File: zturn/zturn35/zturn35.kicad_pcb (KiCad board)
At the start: 4 copper layers, 189.9 x 54 mm, 50 parts, among them U1 74AXP4T245, U10 74AXP4T245, U11 74AXP4T245, U12 74AXP4T245, U2 74AXP4T245, U3 74AXP4T245, U4 74AXP4T245, U5 74AXP4T245, U6 74AXP4T245, U7 74AXP4T245, U8 74AXP4T245, U9 74AXP4T245

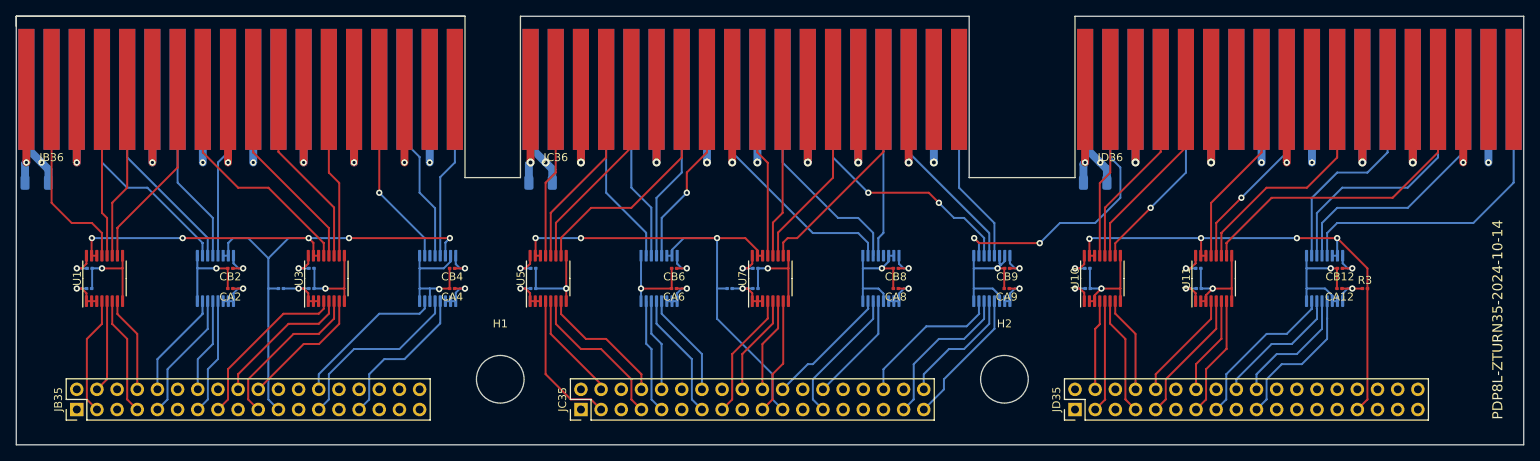
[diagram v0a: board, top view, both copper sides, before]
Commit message: update zturn34,35 pcbs - move 10uF caps, add fiducials
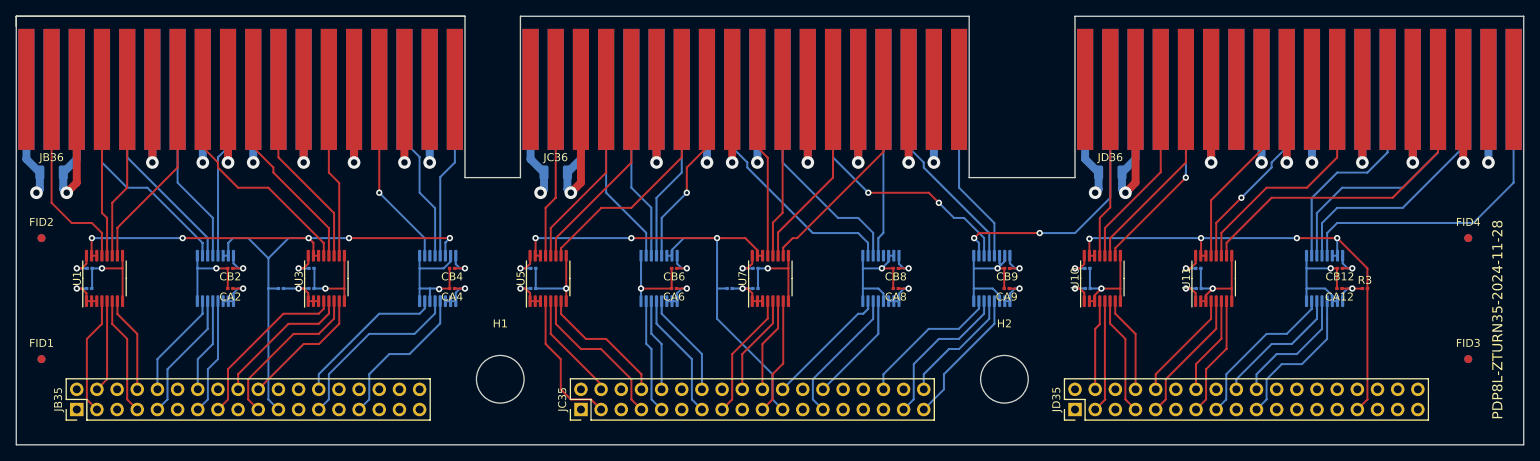
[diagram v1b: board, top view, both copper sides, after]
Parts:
- added FID1: Fiducial, Fiducial:Fiducial_1mm_Mask2mm, F.Cu at (3.17, 43.2)
- added FID2: Fiducial, Fiducial:Fiducial_1mm_Mask2mm, F.Cu at (3.17, 27.9)
- added FID3: Fiducial, Fiducial:Fiducial_1mm_Mask2mm, F.Cu at (182.9, 43.2)
- added FID4: Fiducial, Fiducial:Fiducial_1mm_Mask2mm, F.Cu at (182.9, 27.9)
- added FID5: Fiducial, Fiducial:Fiducial_1mm_Mask2mm, B.Cu at (3.17, 43.2)
- added FID6: Fiducial, Fiducial:Fiducial_1mm_Mask2mm, B.Cu at (3.17, 27.9)
- added FID7: Fiducial, Fiducial:Fiducial_1mm_Mask2mm, B.Cu at (182.9, 43.2)
- added FID8: Fiducial, Fiducial:Fiducial_1mm_Mask2mm, B.Cu at (182.9, 27.9)
- moved C3 2.29 mm to (137.8, 19.7), turned to 0 degrees
- moved C2 2.29 mm to (67.9, 19.7), turned to 0 degrees
- moved C1 2.26 mm to (4.45, 19.7), turned to 0 degrees
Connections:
- JB36 pad A1: GND -> unconnected-(JB36-PadA1)
- JC36 pad A1: GND -> unconnected-(JC36-PadA1)
- JD36 pad A1: GND -> unconnected-(JD36-PadA1)
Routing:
- net +5V: track 78.3 -> 103.3 mm
- net GND: track 433.9 -> 456.9 mm, vias 42 -> 39
- net /pBMB_10: track 33.5 -> 25.9 mm
- net /pBMB_02: track 17.6 -> 24.9 mm
- net /jTHREECYCLE: track 31.4 -> 24.1 mm
- net /jMEM03: track 29.5 -> 22.2 mm
- net /j_DMADATA_05: track 21.5 -> 14.2 mm
- net /j_EXTDMAADD_13: track 25.2 -> 17.9 mm
- net /j_DMADATA_04: track 23.3 -> 16.0 mm
- net /j_DMADATA_02: track 17.6 -> 24.9 mm
- net /jMEM04: track 24.9 -> 17.6 mm
- net /pBMB_07: track 24.6 -> 17.3 mm
- net /jMEM11: track 21.5 -> 14.2 mm
- net /pD35B2: track 37.7 -> 35.4 mm
- net /oD35B2: track 19.1 -> 18.3 mm
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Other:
- board text added: "PDP8L-ZTURN35-2024-11-28"
- board text removed: "PDP8L-ZTURN35-2024-10-14"

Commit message: use transistors for bus drivers instead of chips
to handle the 180 & 220-ohm pullups
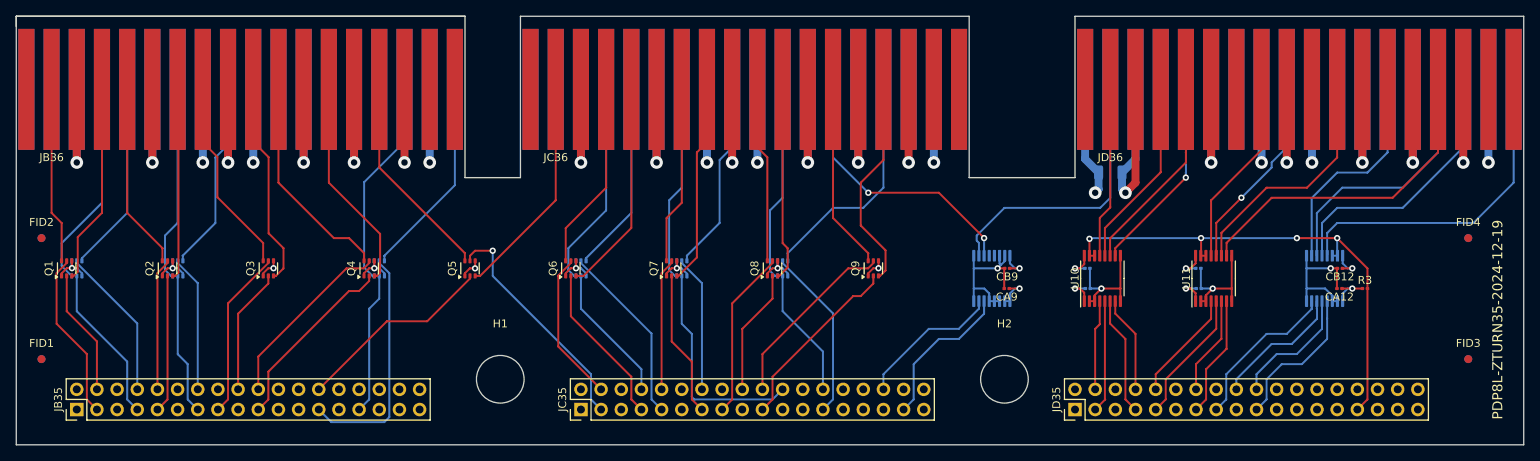
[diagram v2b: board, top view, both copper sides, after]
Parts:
- removed C1, C2: 10u, Capacitor_SMD:C_1206_3216Metric
- removed CA1, CA2, CA3, CA4, CA5, CA6, CA7, CA8, CB1, CB2, CB3, CB4, CB5, CB6, CB7, CB8: 0.1u, Capacitor_SMD:C_0201_0603Metric
- removed R1, R2: 10K, Resistor_SMD:R_0201_0603Metric
- removed U1, U2, U3, U4, U5, U6, U7, U8: 74AXP4T245, Package_SO:TSSOP-16_4.4x5mm_P0.65mm
- added Q1: SSM6N15AFU, Package_TO_SOT_SMD:SOT-363_SC-70-6, F.Cu at (6.35, 31.8)
- added Q10: SSM6N15AFU, Package_TO_SOT_SMD:SOT-363_SC-70-6, B.Cu at (7.62, 31.8)
- added Q11: SSM6N15AFU, Package_TO_SOT_SMD:SOT-363_SC-70-6, B.Cu at (20.3, 31.7)
- added Q12: SSM6N15AFU, Package_TO_SOT_SMD:SOT-363_SC-70-6, B.Cu at (45.7, 31.8)
- added Q13: SSM6N15AFU, Package_TO_SOT_SMD:SOT-363_SC-70-6, B.Cu at (71.1, 31.8)
- added Q14: SSM6N15AFU, Package_TO_SOT_SMD:SOT-363_SC-70-6, B.Cu at (83.8, 31.8)
- added Q15: SSM6N15AFU, Package_TO_SOT_SMD:SOT-363_SC-70-6, B.Cu at (96.5, 31.8)
- added Q2: SSM6N15AFU, Package_TO_SOT_SMD:SOT-363_SC-70-6, F.Cu at (19.1, 31.8)
- added Q3: SSM6N15AFU, Package_TO_SOT_SMD:SOT-363_SC-70-6, F.Cu at (31.8, 31.8)
- added Q4: SSM6N15AFU, Package_TO_SOT_SMD:SOT-363_SC-70-6, F.Cu at (44.5, 31.8)
- added Q5: SSM6N15AFU, Package_TO_SOT_SMD:SOT-363_SC-70-6, F.Cu at (57.1, 31.8)
- added Q6: SSM6N15AFU, Package_TO_SOT_SMD:SOT-363_SC-70-6, F.Cu at (69.8, 31.8)
- added Q7: SSM6N15AFU, Package_TO_SOT_SMD:SOT-363_SC-70-6, F.Cu at (82.5, 31.8)
- added Q8: SSM6N15AFU, Package_TO_SOT_SMD:SOT-363_SC-70-6, F.Cu at (95.2, 31.8)
- added Q9: SSM6N15AFU, Package_TO_SOT_SMD:SOT-363_SC-70-6, F.Cu at (108.0, 31.8)
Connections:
- JB36 pad A2: +5V -> unconnected-(JB36-PadA2)
- JC36 pad A2: +5V -> unconnected-(JC36-PadA2)
- U9 pad 12: /j_EXTDMAADD_13 -> unconnected-(U9-1B2-Pad12)
- U9 pad 13: /j_EXTDMAADD_14 -> unconnected-(U9-1B1-Pad13)
- U9 pad 4: /i_EXTDMAADD_14 -> GND
- U9 pad 5: /i_EXTDMAADD_13 -> GND
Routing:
- net /x_MEM: track 89.1 -> 0.00 mm, vias 5 -> 0
- net GND: track 456.9 -> 371.6 mm, vias 39 -> 40
- net /x_DMADATA: track 66.7 -> 0.00 mm, vias 3 -> 0
- net +5V: track 103.3 -> 37.8 mm, vias 15 -> 5
- net +3V3: track 60.5 -> 16.9 mm, vias 12 -> 4
- net /j_EXTDMAADD_14: track 22.8 -> 0.00 mm
- net /j_EXTDMAADD_13: track 17.9 -> 0.00 mm
- net /i_EXTDMAADD_14: track 17.3 -> 0.00 mm
- net /i_EXTDMAADD_13: track 15.3 -> 0.00 mm
- net /iTHREECYCLE: track 16.0 -> 27.9 mm
- net /DMABUSN: track 11.9 -> 23.4 mm
- net /DMABUSA: track 18.0 -> 29.4 mm, vias 0 -> 1
- net /DMABUSC: track 14.5 -> 22.9 mm
- net /DMABUSF: track 14.7 -> 23.2 mm
- net /j_EXTDMAADD_12: track 21.2 -> 28.8 mm
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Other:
- board text added: "PDP8L-ZTURN35-2024-12-19"
- board text removed: "PDP8L-ZTURN35-2024-11-28"

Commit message: update net names on zturn pcbs to match active high/low signal type
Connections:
- net /_rBMB renamed /r_BMB
- net /_rMA renamed /r_MA
- net /_xINPUTBUS renamed /x_INPUTBUS
- net /iBEMA renamed /i_BEMA
- net /iMEM07 renamed /iMEM_07
- net /iTHREECYCLE renamed /i_3CYCLE
- net /i_INT_RQST renamed /iINT_RQST
- net /jBEMA renamed /j_BEMA
- net /jMEM07 renamed /jMEM_07
- net /jTHREECYCLE renamed /j_3CYCLE
- net /oBWC_OVERFLOW renamed /o_BWC_OVERFLOW
- net /pBWC_OVERFLOW renamed /p_BWC_OVERFLOW

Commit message: update software and further updates to firmware/pcbs
...for invertering transistors

./z8lsimtest works
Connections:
- net /iCA_INCREMENT renamed /i_CA_INCRMNT
- net /iMEM_07 renamed /i_MEM_07
- net /i_3CYCLE renamed /i3CYCLE
- net /i_AC_CLEAR renamed /iAC_CLEAR
- net /i_BEMA renamed /iBEMA
- net /i_EMA renamed /iEMA
- net /i_EXTDMAADD_12 renamed /iEXTDMAADD_12
- net /i_IO_SKIP renamed /iIO_SKIP
- net /jCA_INCREMENT renamed /jCA_INCRMNT
- net /o_B_RUN renamed /oB_RUN
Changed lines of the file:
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@@
   )
   (net 0 "")
-  (net 1 "/jCA_INCREMENT")
+  (net 1 "/jCA_INCRMNT")
   (net 2 "/p_BWC_OVERFLOW")
   (net 3 "/j_EXTDMAADD_12")
@@
   (net 25 "/i_MEMDONE")
   (net 26 "/i_STROBE")
-  (net 27 "/i_BEMA")
-  (net 28 "/i_EMA")
+  (net 27 "/iBEMA")
+  (net 28 "/iEMA")
   (net 29 "/DMABUSA")
   (net 30 "/DMABUSH")
@@
   (net 44 "/oD35B2")
   (net 45 "/DMABUSN")
-  (net 46 "/i_3CYCLE")
-  (net 47 "/iCA_INCREMENT")
-  (net 48 "/i_EXTDMAADD_12")
+  (net 46 "/i3CYCLE")
+  (net 47 "/i_CA_INCRMNT")
+  (net 48 "/iEXTDMAADD_12")
   (net 49 "unconnected-(JC36-PadU1)")
   (net 50 "unconnected-(JC36-PadV1)")
@@
   (net 93 "/pBMB_11")
   (net 94 "/jMEM_P")
-  (net 95 "/i_IO_SKIP")
+  (net 95 "/iIO_SKIP")
   (net 96 "/jMEM00")
   (net 97 "/jMEM08")
@@
   (net 106 "/iINT_RQST")
   (net 107 "/jMEM06")
-  (net 108 "/i_AC_CLEAR")
+  (net 108 "/iAC_CLEAR")
   (net 109 "/i_EA")
   (net 110 "/j_BEMA")
@@
   (net 122 "unconnected-(JB36-PadU1)")
   (net 123 "unconnected-(JB36-PadV1)")
-  (net 124 "/o_B_RUN")
+  (net 124 "/oB_RUN")
   (net 125 "unconnected-(JC36-PadB2)")
   (net 126 "unconnected-(U9-1B1-Pad13)")
   (net 127 "/pD35B2")
-  (net 128 "/iMEM_07")
+  (net 128 "/i_MEM_07")
   (net 129 "/o_BWC_OVERFLOW")
   (net 130 "unconnected-(JD35-Pin_22-Pad22)")
@@
       (net 79 "/j_DMADATA_06") (pinfunction "M1") (pintype "passive"))
     (pad "M2" connect rect (at -22.225 0) (size 2.032 15.24) (layers "B.Cu" "B.Mask")
-      (net 1 "/jCA_INCREMENT") (pinfunction "M2") (pintype "passive"))
+      (net 1 "/jCA_INCRMNT") (pinfunction "M2") (pintype "passive"))
     (pad "N1" connect rect (at -19.05 0) (size 2.032 15.24) (layers "F.Cu" "F.Mask")
       (net 31 "GND") (pinfunction "N1") (pintype "passive"))
@@
       (net 118 "/x_DMADATA") (pinfunction "Pin_21") (pintype "passive"))
     (pad "22" thru_hole oval (at 2.54 25.4 90) (size 1.7 1.7) (drill 1) (layers "*.Cu" "*.Mask")
-      (net 46 "/i_3CYCLE") (pinfunction "Pin_22") (pintype "passive"))
+      (net 46 "/i3CYCLE") (pinfunction "Pin_22") (pintype "passive"))
     (pad "23" thru_hole oval (at 0 27.94 90) (size 1.7 1.7) (drill 1) (layers "*.Cu" "*.Mask")
       (net 31 "GND") (pinfunction "Pin_23") (pintype "passive"))
@@
       (net 31 "GND") (pinfunction "Pin_24") (pintype "passive"))
     (pad "25" thru_hole oval (at 0 30.48 90) (size 1.7 1.7) (drill 1) (layers "*.Cu" "*.Mask")
-      (net 47 "/iCA_INCREMENT") (pinfunction "Pin_25") (pintype "passive"))
+      (net 47 "/i_CA_INCRMNT") (pinfunction "Pin_25") (pintype "passive"))
     (pad "26" thru_hole oval (at 2.54 30.48 90) (size 1.7 1.7) (drill 1) (layers "*.Cu" "*.Mask")
-      (net 48 "/i_EXTDMAADD_12") (pinfunction "Pin_26") (pintype "passive"))
+      (net 48 "/iEXTDMAADD_12") (pinfunction "Pin_26") (pintype "passive"))
     (pad "27" thru_hole oval (at 0 33.02 90) (size 1.7 1.7) (drill 1) (layers "*.Cu" "*.Mask")
       (net 31 "GND") (pinfunction "Pin_27") (pintype "passive"))
@@
       (net 133 "/r_BMB") (pinfunction "Pin_29") (pintype "passive"))
     (pad "30" thru_hole oval (at 2.54 35.56 90) (size 1.7 1.7) (drill 1) (layers "*.Cu" "*.Mask")
-      (net 95 "/i_IO_SKIP") (pinfunction "Pin_30") (pintype "passive"))
+      (net 95 "/iIO_SKIP") (pinfunction "Pin_30") (pintype "passive"))
     (pad "31" thru_hole oval (at 0 38.1 90) (size 1.7 1.7) (drill 1) (layers "*.Cu" "*.Mask")
       (net 31 "GND") (pinfunction "Pin_31") (pintype "passive"))
@@
       (net 106 "/iINT_RQST") (pinfunction "Pin_32") (pintype "passive"))
     (pad "33" thru_hole oval (at 0 40.64 90) (size 1.7 1.7) (drill 1) (layers "*.Cu" "*.Mask")
-      (net 108 "/i_AC_CLEAR") (pinfunction "Pin_33") (pintype "passive"))
+      (net 108 "/iAC_CLEAR") (pinfunction "Pin_33") (pintype "passive"))
     (pad "34" thru_hole oval (at 2.54 40.64 90) (size 1.7 1.7) (drill 1) (layers "*.Cu" "*.Mask")
       (net 31 "GND") (pinfunction "Pin_34") (pintype "passive"))
@@
       (net 112 "unconnected-(JD35-Pin_35-Pad35)") (pinfunction "Pin_35") (pintype "passive"))
     (pad "36" thru_hole oval (at 2.54 43.18 90) (size 1.7 1.7) (drill 1) (layers "*.Cu" "*.Mask")
-      (net 124 "/o_B_RUN") (pinfunction "Pin_36") (pintype "passive"))
+      (net 124 "/oB_RUN") (pinfunction "Pin_36") (pintype "passive"))
     (model "${KICAD6_3DMODEL_DIR}/Connector_PinHeader_2.54mm.3dshapes/PinHeader_2x18_P2.54mm_Vertical.wrl"
       (offset (xyz 0 0 0))
@@
       (net 31 "GND") (pinfunction "Pin_24") (pintype "passive"))
     (pad "25" thru_hole oval (at 0 30.48 90) (size 1.7 1.7) (drill 1) (layers "*.Cu" "*.Mask")
-      (net 27 "/i_BEMA") (pinfunction "Pin_25") (pintype "passive"))
+      (net 27 "/iBEMA") (pinfunction "Pin_25") (pintype "passive"))
     (pad "26" thru_hole oval (at 2.54 30.48 90) (size 1.7 1.7) (drill 1) (layers "*.Cu" "*.Mask")
-      (net 128 "/iMEM_07") (pinfunction "Pin_26") (pintype "passive"))
+      (net 128 "/i_MEM_07") (pinfunction "Pin_26") (pintype "passive"))
     (pad "27" thru_hole oval (at 0 33.02 90) (size 1.7 1.7) (drill 1) (layers "*.Cu" "*.Mask")
       (net 31 "GND") (pinfunction "Pin_27") (pintype "passive"))
@@
       (net 31 "GND") (pinfunction "Pin_28") (pintype "passive"))
     (pad "29" thru_hole oval (at 0 35.56 90) (size 1.7 1.7) (drill 1) (layers "*.Cu" "*.Mask")
-      (net 28 "/i_EMA") (pinfunction "Pin_29") (pintype "passive"))
+      (net 28 "/iEMA") (pinfunction "Pin_29") (pintype "passive"))
     (pad "30" thru_hole oval (at 2.54 35.56 90) (size 1.7 1.7) (drill 1) (layers "*.Cu" "*.Mask")
       (net 109 "/i_EA") (pinfunction "Pin_30") (pintype "passive"))
@@
       (net 31 "GND") (pinfunction "S1") (pintype "passive"))
     (pad "2" smd roundrect (at -0.95 0 90) (size 0.65 0.4) (layers "F.Cu" "F.Paste" "F.Mask") (roundrect_rratio 0.25)
-      (net 128 "/iMEM_07") (pinfunction "G1") (pintype "passive"))
+      (net 128 "/i_MEM_07") (pinfunction "G1") (pintype "passive"))
     (pad "3" smd roundrect (at -0.95 0.65 90) (size 0.65 0.4) (layers "F.Cu" "F.Paste" "F.Mask") (roundrect_rratio 0.25)
       (net 69 "/j_DMADATA_00") (pinfunction "D2") (pintype "passive"))
@@
       (net 31 "GND") (pinfunction "S1") (pintype "passive"))
     (pad "2" smd roundrect (at -0.95 0 90) (size 0.65 0.4) (layers "B.Cu" "B.Paste" "B.Mask") (roundrect_rratio 0.25)
-      (net 46 "/i_3CYCLE") (pinfunction "G1") (pintype "passive"))
+      (net 46 "/i3CYCLE") (pinfunction "G1") (pintype "passive"))
     (pad "3" smd roundrect (at -0.95 -0.65 90) (size 0.65 0.4) (layers "B.Cu" "B.Paste" "B.Mask") (roundrect_rratio 0.25)
       (net 75 "/j_DMADATA_11") (pinfunction "D2") (pintype "passive"))
@@
       (net 31 "GND") (pinfunction "S1") (pintype "passive"))
     (pad "2" smd roundrect (at -0.95 0 90) (size 0.65 0.4) (layers "B.Cu" "B.Paste" "B.Mask") (roundrect_rratio 0.25)
-      (net 28 "/i_EMA") (pinfunction "G1") (pintype "passive"))
+      (net 28 "/iEMA") (pinfunction "G1") (pintype "passive"))
     (pad "3" smd roundrect (at -0.95 -0.65 90) (size 0.65 0.4) (layers "B.Cu" "B.Paste" "B.Mask") (roundrect_rratio 0.25)
       (net 110 "/j_BEMA") (pinfunction "D2") (pintype "passive"))
@@
       (net 31 "GND") (pinfunction "S2") (pintype "passive"))
     (pad "5" smd roundrect (at 0.95 0 90) (size 0.65 0.4) (layers "B.Cu" "B.Paste" "B.Mask") (roundrect_rratio 0.25)
-      (net 27 "/i_BEMA") (pinfunction "G2") (pintype "passive"))
+      (net 27 "/iBEMA") (pinfunction "G2") (pintype "passive"))
     (pad "6" smd roundrect (at 0.95 0.65 90) (size 0.65 0.4) (layers "B.Cu" "B.Paste" "B.Mask") (roundrect_rratio 0.25)
       (net 113 "/j_EMA") (pinfunction "D1") (pintype "passive"))
@@
       (net 31 "GND") (pinfunction "S1") (pintype "passive"))
     (pad "2" smd roundrect (at -0.95 0 90) (size 0.65 0.4) (layers "B.Cu" "B.Paste" "B.Mask") (roundrect_rratio 0.25)
-      (net 48 "/i_EXTDMAADD_12") (pinfunction "G1") (pintype "passive"))
+      (net 48 "/iEXTDMAADD_12") (pinfunction "G1") (pintype "passive"))
     (pad "3" smd roundrect (at -0.95 -0.65 90) (size 0.65 0.4) (layers "B.Cu" "B.Paste" "B.Mask") (roundrect_rratio 0.25)
-      (net 1 "/jCA_INCREMENT") (pinfunction "D2") (pintype "passive"))
+      (net 1 "/jCA_INCRMNT") (pinfunction "D2") (pintype "passive"))
     (pad "4" smd roundrect (at 0.95 -0.65 90) (size 0.65 0.4) (layers "B.Cu" "B.Paste" "B.Mask") (roundrect_rratio 0.25)
       (net 31 "GND") (pinfunction "S2") (pintype "passive"))
     (pad "5" smd roundrect (at 0.95 0 90) (size 0.65 0.4) (layers "B.Cu" "B.Paste" "B.Mask") (roundrect_rratio 0.25)
-      (net 47 "/iCA_INCREMENT") (pinfunction "G2") (pintype "passive"))
+      (net 47 "/i_CA_INCRMNT") (pinfunction "G2") (pintype "passive"))
     (pad "6" smd roundrect (at 0.95 0.65 90) (size 0.65 0.4) (layers "B.Cu" "B.Paste" "B.Mask") (roundrect_rratio 0.25)
       (net 3 "/j_EXTDMAADD_12") (pinfunction "D1") (pintype "passive"))
